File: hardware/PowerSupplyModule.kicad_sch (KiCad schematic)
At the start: 131 parts, among them J1 Conn_01x02_Socket, J2 Conn_01x02_Socket, J3 Conn_01x08_Pin, J4 Conn_ARM_SWD_TagConnect_TC203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, K1 AZ576-1C-24DE, K2 AZ576-1A-24DE, K3 AZ576-1A-24DE, K4 AZ576-1A-24DE, Q3 IPZ40N04S5L4R8ATMA1, SW1 1825910-6, U16 AT24CS08-SSHM, U17 STM32C031K4Tx, U18 SN74LVC1G08, U19 TPL7407LPWR, U20 SN74LVC1G08, U21 MIC826, U22 ISO1540, U23 SI8652EB-B-IU

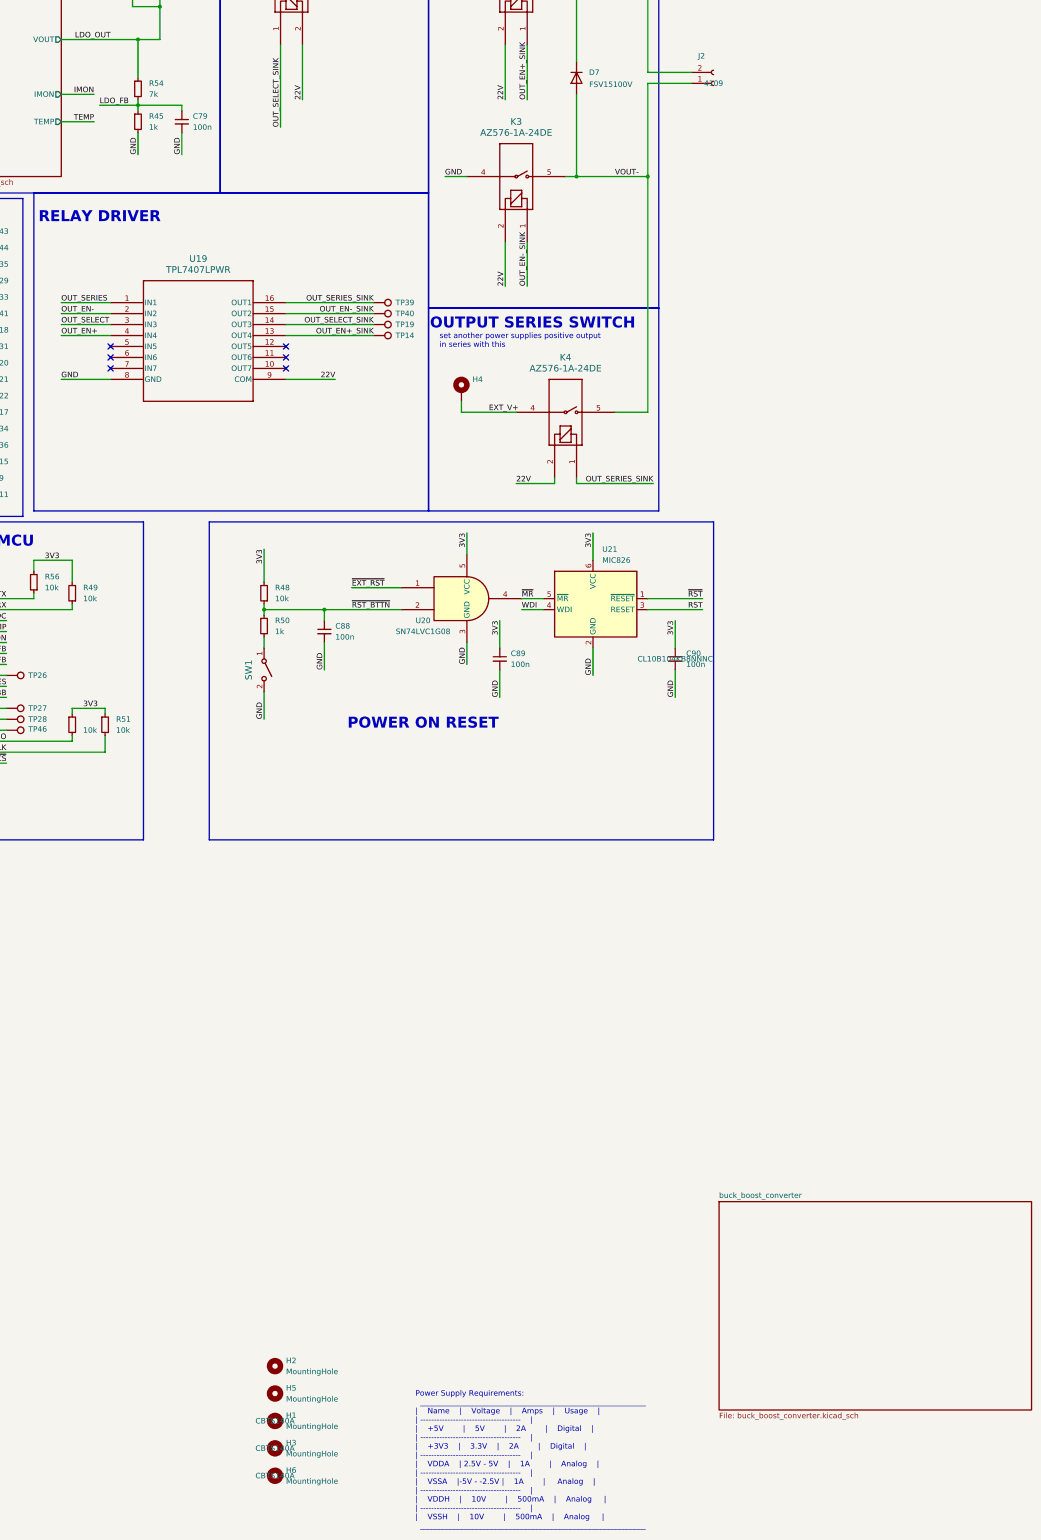
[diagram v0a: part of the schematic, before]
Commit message: fixed kicad project errors
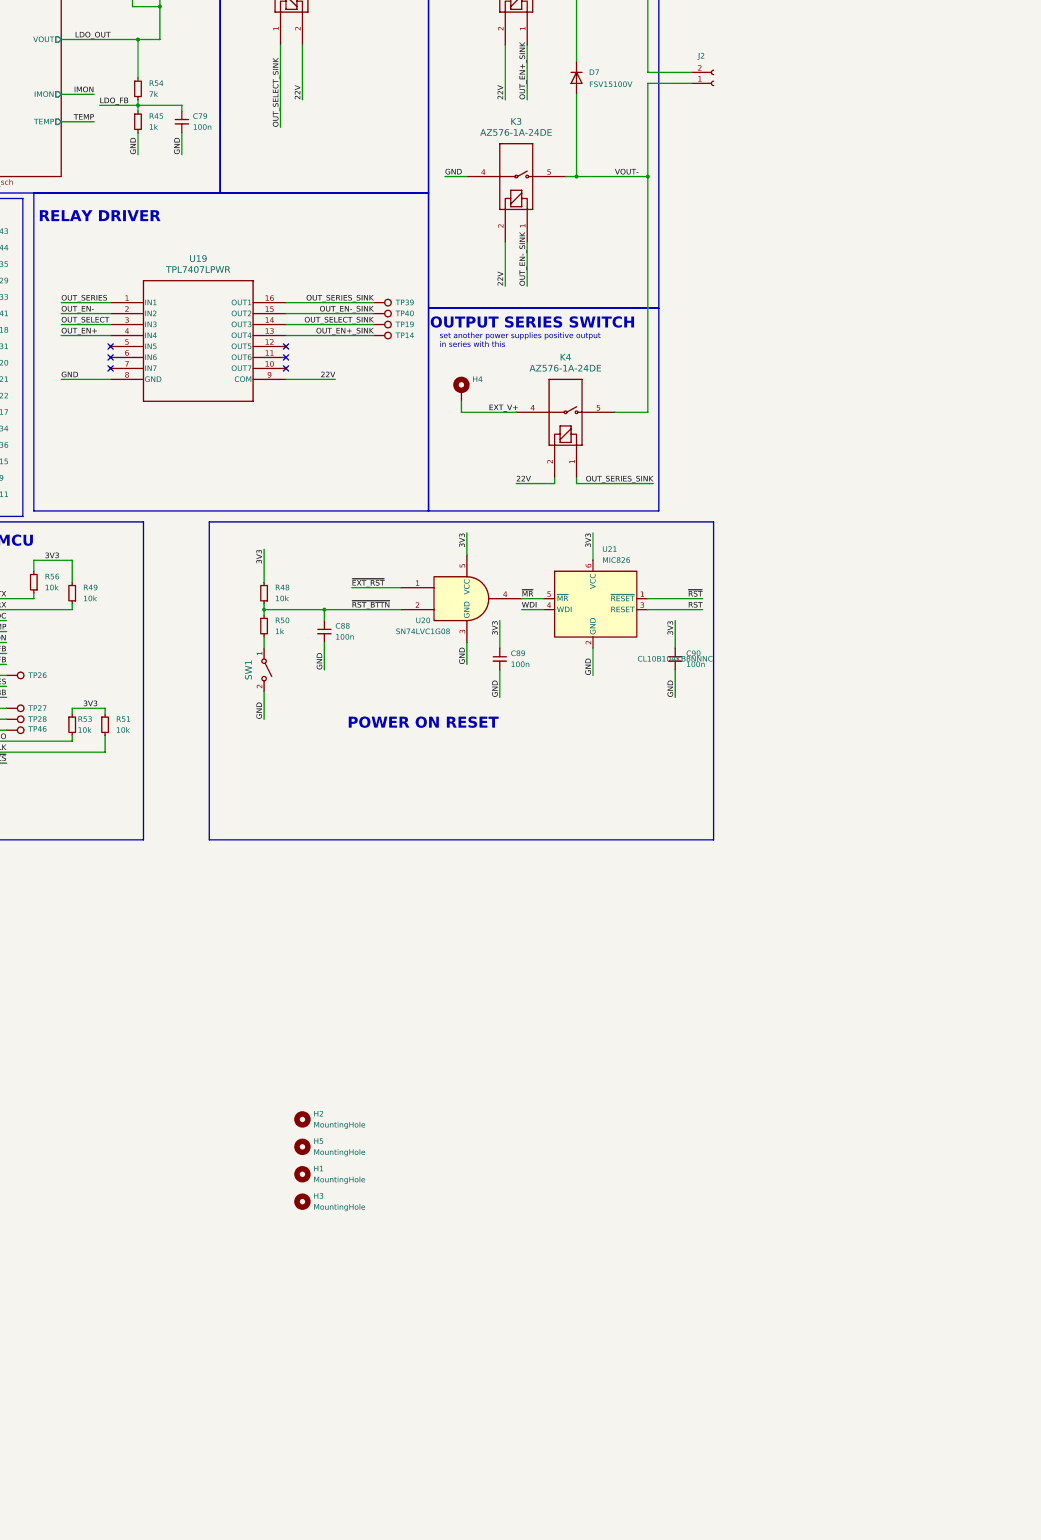
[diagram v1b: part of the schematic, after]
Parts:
- removed H6: MountingHole, Library:MountingHole_3.5mm, symbol Library:MountingHole
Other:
- removed sheet buck_boost_converter
- note removed: "Power Supply Requirements: ____________________________________________________________ | Name | Voltage | Amps | Usage | | ------------------------------------- | | +5V | 5V | 2A | Digital | | ------------------------------------- | | +3V3 | 3.3V | 2A | Digital | | ------------------------------------- | | VDDA | 2.5V - 5V | 1A | Analog | | ------------------------------------- | | VSSA |-5V - -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"
- moved on the sheet: H1, H2, H3, H5
